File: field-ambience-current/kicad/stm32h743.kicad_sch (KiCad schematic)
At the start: 22 parts, among them J9 JST PH 2.0 2-pin (LiPo Batter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, Q1 DMG2305UX P-MOS SOT-23 (USB-C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, U7 MCP73831T-2ACI/OT (LiPo Charg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, U8 TPS61089RNR (Boost LiPo→5V, 2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

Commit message: pcb(r18.5): Schematic-Migration Phase 3 — STM32H743 + LCD im Generator, Repo-Audit-Fixes
KERN: generate_kicad_project.py erzeugt jetzt die H7-Architektur.

NEU stm32h743.kicad_sch (ersetzt pico.kicad_sch -> kicad/legacy_pico2/):
- 100-Pin-Symbol 1:1 aus offizieller KiCad-Lib (MCU_ST_STM32H7),
  doppelt verifiziert gegen SPEC v0.7 §5 / DS12110 Rev 5 Table 8 —
  alle 52 belegten Zuordnungen identisch (zwei unabhängige Quellen)
- alle SPEC-§5-Netze verdrahtet, 48 Reserve-GPIOs no_connect
- Support: HSE Y1 ABLS-8.000MHZ-B4-T (C596838) + 2x22pF, VCAP 2x2.2uF
  (DS12110 Tab.24), 5x(4.7uF+100nF) VDD-Bank, VDDA-Ferrit C84094 +
  1uF+100nF, BOOT0-PD 10k, NRST-PU 10k+100nF, SWD-J4 (PA13/PA14/GND),
  BAT-Teiler 100k/100k+10nF an PA3, Status-LED PD8, USB-FS PA11/PA12
  (USBLC6-ESD bleibt davor), MIDI_TX-Netz (PD5)

NEU lcd.kicad_sch (ersetzt oled.kicad_sch -> legacy): 8-Pin-ST7789
per SPEC §6 + C6b/C6c + Backlight: PCA9685-Kanal-12 -> LCD_BLK_PWM ->
2N7002 Low-Side + 100k-PD. Netze OLED_* -> LCD_*.

power_tree: U5 AP7361A-33 LDO (+5V->+3V3) + Cin 1uF/Cout 2.2uF +
EN->IN. Pico-SMPS entfällt. PICO_USB_* -> USB_DM/USB_DP.

mcp: GPB5 = VOL_SW (SPEC §5.4 — lag bis r17 entgegen der SPEC am
Pico-GPIO), PCA-Kanal 12 = LCD_BLK_PWM. Root-Brücken umgebaut,
kicad_pro-Sheetliste: Battery ergänzt (fehlte).

AUDIT-FINDINGS (verifiziert, nicht aus dem Alt-Audit übernommen):
- F-6 NEU 🔴: SPEC-§4-U5-LCSC C156144 ist ein 910R-WIDERSTAND
  (LCSC-Web verifiziert) — hätte bei JLC einen R als LDO bestückt.
  SPEC korrigiert (Kandidat C150719), Symbol trägt TBD-VERIFY.
- B-LDO 🔴: AP7361A-SOT-89-5-Pinout-Annahme (1=ADJ/NC,2=OUT,3=IN,
  4=GND,5=EN aus AP7361-DS33626-Lesart; A-Datasheet war HTTP 403) —
  als PIN_VERIFY am Symbol + PCB_LAYOUT_STATUS dokumentiert.
- B-SW12 🔴: SW6-10 (HX 12x12) auf ~6mm-TL3342-Pattern — als
  FP_MISMATCH-Property an allen 5 Symbolen markiert.
- F-2-Teilfix: Encoder-MPN -> EC11J1525402, Bourns-PEC11R-PDF nach
  datasheets/legacy/ (falsches Teil); ALPS-Drawing offen.
- F-1: T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
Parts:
- removed C_BAT_HF: 100nF X7R 0603 (Battery-Input HF), Capacitor_SMD:C_0603_1608Metric, symbol Device:C
- removed C_BAT_IN: 22uF X5R 0805 (Battery-Input Bulk), Capacitor_SMD:C_0805_2012Metric, symbol Device:C
- removed C_BOOST_HF: 100nF X7R 0603 (Boost-Output HF), Capacitor_SMD:C_0603_1608Metric, symbol Device:C
- removed C_BOOST_OUT: 22uF X5R 0805 (Boost-Output Bulk), Capacitor_SMD:C_0805_2012Metric, symbol Device:C
- removed C_BOOT: 100nF X7R 0603 (TPS61089 BOOT-SW cap), Capacitor_SMD:C_0603_1608Metric, symbol Device:C
- removed C_COMP: 1nF X7R 0603 (TPS61089 loop-compensation series), Capacitor_SMD:C_0603_1608Metric, symbol Device:C
- removed C_VCC: 1uF X7R 0603 (TPS61089 internal LDO decoupling, d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, Capacitor_SMD:C_0603_1608Metric, symbol Device:C
- removed D3: SS34 40V 3A Schottky (Boost-Out Reverse-Protect), Diode_SMD:D_SMA, symbol Device:D_Schottky
- removed J9: JST PH 2.0 2-pin (LiPo Battery, r9), Connector_JST:JST_PH_S2B-PH-SM4-TB_1x02-1MP_P2.00mm_Horizontal, symbol Connector:Conn_01x02
- removed L1: 2.2uH 5A Shielded 0630 (TPS61089 Boost Inductor), Inductor_SMD:L_0630_6.0x6.0mm, symbol Device:L
- removed LED_CHRG: 0603 amber (LiPo Charging indicator), LED_SMD:LED_0603_1608Metric, symbol Device:LED
- removed Q1: DMG2305UX P-MOS SOT-23 (USB-C Power-Path-Switch), Package_TO_SOT_SMD:SOT-23, symbol Transistor_FET:DMG2305UX
- removed R21: 2k 0603 (MCP73831 R_PROG → 500mA Icharge), Resistor_SMD:R_0603_1608Metric, symbol Device:R
- removed R22: 10k 0603 (Q1 Gate Pull-Down, Default-OFF), Resistor_SMD:R_0603_1608Metric, symbol Device:R
- removed R23: 200k 0603 (TPS61089 FB-Divider Top, Vout=5V targe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, Resistor_SMD:R_0603_1608Metric, symbol Device:R
- removed R24: 39k 0603 (TPS61089 FB-Divider Bottom), Resistor_SMD:R_0603_1608Metric, symbol Device:R
- removed R_CHRG: 1k 0603 (LED_CHRG series), Resistor_SMD:R_0603_1608Metric, symbol Device:R
- removed R_COMP: 22k 0603 (TPS61089 loop-compensation), Resistor_SMD:R_0603_1608Metric, symbol Device:R
- removed R_FSW: 360k 0603 1% (TPS61089 Fsw-Set ~1.21MHz, r12-B11), Resistor_SMD:R_0603_1608Metric, symbol Device:R
- removed R_ILIM: 20k 0603 1% (TPS61089 current-limit ~4A peak), Resistor_SMD:R_0603_1608Metric, symbol Device:R
- removed U7: MCP73831T-2ACI/OT (LiPo Charger, 500mA via R21=2k), Package_TO_SOT_SMD:SOT-23-5, symbol Battery:MCP73831
- removed U8: TPS61089RNR (Boost LiPo→5V, 2A, programmable Fsw), Package_DFN_QFN:VQFN-11-1EP_2.6x2.6mm_P0.5mm_EP0.85x1.5mm_HotRod, symbol Regulator_Switching:TPS61089
- added C_BAT_FILT: 10nF X7R 0603 (ADC S/H filter), Capacitor_SMD:C_0603_1608Metric, symbol Device:C
- added C_HSE1, C_HSE2: 22pF C0G/NP0 0603 (HSE load, Startwert §5.9), Capacitor_SMD:C_0603_1608Metric, symbol Device:C
- added C_NRST: 100nF X7R 0603 (NRST debounce), Capacitor_SMD:C_0603_1608Metric, symbol Device:C
- added C_VCAP1, C_VCAP2: 2.2uF X5R 0603, ESR<100mOhm (VCAP, DS12110 Tab.24), Capacitor_SMD:C_0603_1608Metric, symbol Device:C
- added C_VDD1A, C_VDD2A, C_VDD3A, C_VDD4A, C_VDD5A: 4.7uF X5R 0805 (VDD bulk), Capacitor_SMD:C_0805_2012Metric, symbol Device:C
- added C_VDD1B, C_VDD2B, C_VDD3B, C_VDD4B, C_VDD5B: 100nF X7R 0603 (VDD HF), Capacitor_SMD:C_0603_1608Metric, symbol Device:C
- added C_VDDA1: 1uF X5R 0603 (VDDA), Capacitor_SMD:C_0603_1608Metric, symbol Device:C
- added C_VDDA2: 100nF X7R 0603 (VDDA), Capacitor_SMD:C_0603_1608Metric, symbol Device:C
- added FB2: BLM18AG601 600R@100MHz (VDDA-Filter), Inductor_SMD:L_0603_1608Metric, symbol Device:Ferrite_Bead
- added J4: SWD 1.27mm (SWCLK/GND/SWDIO), Connector_PinHeader_1.27mm:PinHeader_1x03_P1.27mm_Vertical, symbol Connector:Conn_01x03
- added LED_HB: 0603 warm-white (heartbeat), LED_SMD:LED_0603_1608Metric, symbol Device:LED
- added R_BAT_DIV_BOT: 100k 0603 (BAT divider bottom), Resistor_SMD:R_0603_1608Metric, symbol Device:R
- added R_BAT_DIV_TOP: 100k 0603 (BAT divider top), Resistor_SMD:R_0603_1608Metric, symbol Device:R
- added R_BOOT0: 10k 0603 (BOOT0 pull-down), Resistor_SMD:R_0603_1608Metric, symbol Device:R
- added R_NRST: 10k 0603 (NRST pull-up), Resistor_SMD:R_0603_1608Metric, symbol Device:R
- added R_SLED: 820R 0603 (status LED), Resistor_SMD:R_0603_1608Metric, symbol Device:R
- added U1: STM32H743VIT6 (480MHz M7, LQFP-100), Package_QFP:LQFP-100_14x14mm_P0.5mm, symbol MCU:STM32H743VIT6
- added Y1: 8MHz ABLS-8.000MHZ-B4-T (CL=18pF, ESR<=80R), Crystal:Crystal_SMD_HC49-SD, symbol Device:Crystal
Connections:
- net BAT_PLUS: now also R_BAT_DIV_TOP.1
- net GND: now also C_BAT_FILT.2, C_HSE1.2, C_HSE2.2, C_NRST.2, C_VCAP1.2, C_VCAP2.2, C_VDD1A.2, C_VDD1B.2, C_VDD2A.2, C_VDD2B.2, C_VDD3A.2, C_VDD3B.2, C_VDD4A.2, C_VDD4B.2, C_VDD5A.2, C_VDD5B.2, C_VDDA1.2, C_VDDA2.2, LED_HB.1 (K), R_BAT_DIV_BOT.2, R_BOOT0.2
- new net: LED_HB.2 (A), R_SLED.2
- new net +3V3: C_VDD1A.1, C_VDD1B.1, C_VDD2A.1, C_VDD2B.1, C_VDD3A.1, C_VDD3B.1, C_VDD4A.1, C_VDD4B.1, C_VDD5A.1, C_VDD5B.1, R_NRST.1
- new net BAT_SENSE: C_BAT_FILT.1, R_BAT_DIV_BOT.1, R_BAT_DIV_TOP.2
- new net BOOT0_PIN: R_BOOT0.1
- new net HSE_IN: C_HSE1.1, Y1.1
- new net HSE_OUT: C_HSE2.1, Y1.2
- new net NRST: C_NRST.1, R_NRST.2
- new net STATUS_LED: R_SLED.1
- new net VDDA_3V3: C_VDDA1.1, C_VDDA2.1
- no-connect marks 0 -> 49
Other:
- note added: "MIDI_TX (PD5): Netz vorhanden, TRS-Type-A-Buchse + Serien-R fehlen im Design — SPEC §4 hat keine Buchsen-Zeile. BLOCKER B-MIDI in PCB_TODO.md (MIDI-1.0-3V3-Spec: 10R/33R)."
- note added: "SWO (PB3): optionaler Trace-Pin, bewusst nur Label (ERC-Info erwartet)."
- title: Field Ambience PCB — Sheet 7: Battery & Power-Path (r9 + r12) -> Field Ambience — Sheet 2: STM32H743 (r18 H7-Migration)

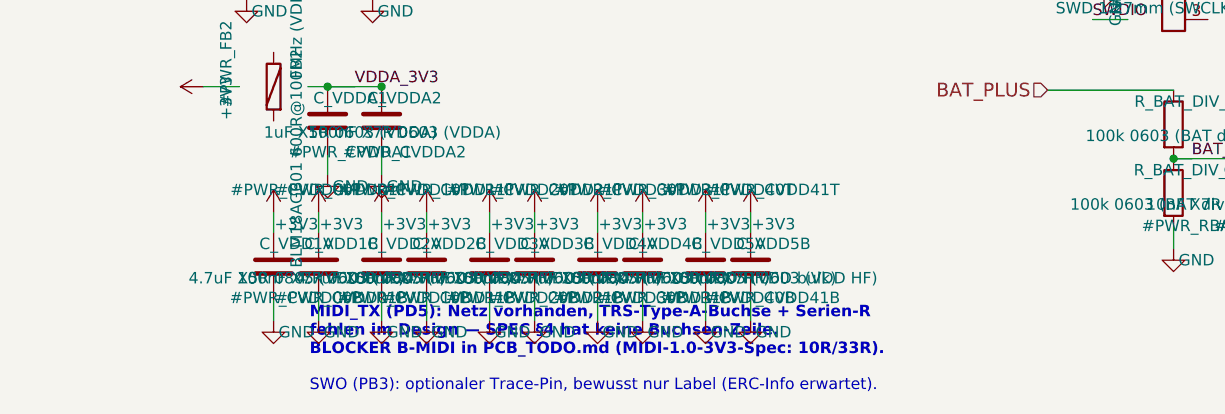
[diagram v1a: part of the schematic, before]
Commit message: pcb(r18.6): Engineering-Verifikation — AP7361C-Pinout-Fix, TPS61089-Quelle, Custom-FP, BOM-LCSC, ADR-MIDI
Reaktion auf User-Korrekturen aus öffentlichen Datasheets. Vier
🔴-Blocker geschlossen, einer auf eine Design-Entscheidung umklassifiziert.

=== AP7361A-Pinout war FALSCH — gefixt + AP7361C ===

r18.5-Annahme: 1=ADJ/NC, 2=OUT, 3=IN, 4=GND, 5=EN.
Korrekt (Diodes-DS via mouser.de/datasheet/3/175/1/AP7361.pdf,
User-verifiziert):
    1=EN, 2=GND, 3=ADJ/NC, 4=IN, 5=OUT

Hätte zu einem totem Board geführt (IN/OUT/EN vertauscht).

Zusätzlich:
- Symbol auf AP7361C umbenannt (Diodes markiert AP7361 als NRND ->
  use AP7361C; gleicher SOT-89-5-Pinout)
- AP7361C-33Y5-13 = LCSC C460397 (SOT-89-5) statt r18.5-Kandidat
  C150719 (= SOT-223, falsches Package; verworfen)
- Cin/Cout 4.7 µF X5R 0603 (DS-Empfehlung, statt 1µF/2.2µF)
- Symbol-Pinmap + power_tree-Verdrahtung umgebaut: EN-Pin liegt
  jetzt links oben (statt links unten), IN links unten, OUT
  rechts oben — neu gerechnete Stub-Wires + Junctions

=== TPS61089-Footprint + Datenblatt-Anchor ===

- Symbol-Pinmap (1=FSW … 11=SW) verifiziert gegen TI Rev C Tabelle 6-1
  (User-Quelle ti.com/lit/gpn/tps61089) — als PIN_SOURCE-Property
- Footprint-Name auf RNR0011A-Konvention 2.0x2.5mm VQFN-HR
- RNSR-PDF → datasheets/legacy/TPS61089RNSR_wrong_variant.pdf

=== Encoder C209762 (NRND, Prototype-OK) ===

- MPN EC11J1525402, LCSC C209762 (JLCPCB-verifiziert)
- Datasheet-Link auf JLCPCB-Detail-Seite (ALPS-Drawing nicht öffentlich)
- Status: NRND als Property — Prototype-OK, Serie braucht Ersatztyp
- FP_VERIFY-Hinweis (EC11J ist SMD, der KiCad-Standard-FP EC11E ist THT)

=== Custom-Footprint für HX 12x12 (SW6-10) ===

- libraries/field_ambience.pretty/SW_HX_12x12x7.3_SMD-4P.kicad_mod
  basierend auf LCSC-Daten von C36498966:
  - SMD-4P, 11.8x11.8mm Body, 7.3mm Höhe
  - 4 Pads je 2.5x1.5mm auf 7mm-Pitch (X+Y)
  - SPST: gegenüberliegende Pads verbunden (1↔1, 2↔2)
  - Silkscreen + Pin-1-Dot + Courtyard +0.25mm IPC-7351B
- fp-lib-table um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
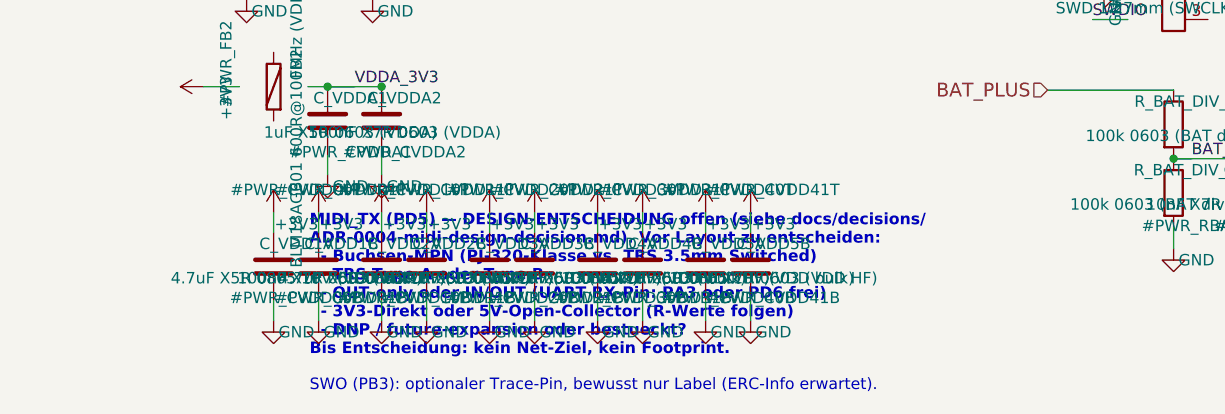
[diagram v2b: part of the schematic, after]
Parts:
- C_HSE1, C_HSE2: LCSC TBD-VERIFY -> C1804; MPN TBD-VERIFY (22pF C0G 50V 0603) -> CC0603JRNPO9BN220; Manufacturer (none) -> Yageo; VERIFY-STOCK (none) -> 22pF +-5% C0G/NP0 50V 0603
- C_VCAP1, C_VCAP2: LCSC TBD-VERIFY -> C24539; MPN TBD-VERIFY (2.2uF/6.3V X5R 0603) -> CL10A225KP8NNNC; Manufacturer (none) -> Samsung; VERIFY-STOCK (none) -> JLC Extended 2.2uF/10V X5R 0603 — falls out-of-stock altern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
- C_VDD1A, C_VDD2A, C_VDD3A, C_VDD4A, C_VDD5A: value 4.7uF X5R 0805 (VDD bulk) -> 4.7uF X5R 0805 10V (VDD bulk); LCSC TBD-VERIFY -> C45783; MPN TBD-VERIFY (4.7uF/10V X5R 0805) -> CL21A475KQFNNNE
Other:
- note added: "MIDI_TX (PD5) — DESIGN-ENTSCHEIDUNG offen (siehe docs/decisions/ ADR-0004-midi-design-decision.md). Vor Layout zu entscheiden: - Buchsen-MPN (PJ-320-Klasse vs. TRS 3.5mm Switched) - TRS Type A oder Type B - OUT-only oder IN/OUT (UART RX-Pin: PA3 oder PD6 frei) - 3V3-Direkt oder 5V-Open-Collector (R-Werte folgen) - DNP / future-expansion oder bestueckt? Bis Entscheidung: kein Net-Ziel, kein Footpr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"
- note removed: "MIDI_TX (PD5): Netz vorhanden, TRS-Type-A-Buchse + Serien-R fehlen im Design — SPEC §4 hat keine Buchsen-Zeile. BLOCKER B-MIDI in PCB_TODO.md (MIDI-1.0-3V3-Spec: 10R/33R)."
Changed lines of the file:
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@@
       (property "Datasheet" "~" (at 112.14 83.01 0)
         (effects (font (size 1.27 1.27)) hide))
-      (property "MPN" "TBD-VERIFY (2.2uF/6.3V X5R 0603)" (at 114.68 86.82000000000001 0)
-        (effects (font (size 1.27 1.27)) hide))
-      (property "LCSC" "TBD-VERIFY" (at 114.68 88.09 0)
+      (property "MPN" "CL10A225KP8NNNC" (at 114.68 86.82000000000001 0)
+        (effects (font (size 1.27 1.27)) hide))
+      (property "Manufacturer" "Samsung" (at 114.68 88.09 0)
+        (effects (font (size 1.27 1.27)) hide))
+      (property "LCSC" "C24539" (at 114.68 89.36 0)
+        (effects (font (size 1.27 1.27)) hide))
+      (property "VERIFY-STOCK" "JLC Extended 2.2uF/10V X5R 0603 — falls out-of-stock alternative LCSC-Nr. waehlen" (at 114.68 90.63000000000001 0)
         (effects (font (size 1.27 1.27)) hide))
     (instances
@@
       (property "Datasheet" "~" (at 112.14 85.55 0)
         (effects (font (size 1.27 1.27)) hide))
-      (property "MPN" "TBD-VERIFY (2.2uF/6.3V X5R 0603)" (at 114.68 89.36 0)
-        (effects (font (size 1.27 1.27)) hide))
-      (property "LCSC" "TBD-VERIFY" (at 114.68 90.63 0)
+      (property "MPN" "CL10A225KP8NNNC" (at 114.68 89.36 0)
+        (effects (font (size 1.27 1.27)) hide))
+      (property "Manufacturer" "Samsung" (at 114.68 90.63 0)
+        (effects (font (size 1.27 1.27)) hide))
+      (property "LCSC" "C24539" (at 114.68 91.89999999999999 0)
+        (effects (font (size 1.27 1.27)) hide))
+      (property "VERIFY-STOCK" "JLC Extended 2.2uF/10V X5R 0603 — falls out-of-stock alternative LCSC-Nr. waehlen" (at 114.68 93.17 0)
         (effects (font (size 1.27 1.27)) hide))
     (instances
@@
       (property "Reference" "C_VDD1A" (at 98.54 235.46 0)
         (effects (font (size 1.27 1.27))))
-      (property "Value" "4.7uF X5R 0805 (VDD bulk)" (at 98.54 239.27 0)
+      (property "Value" "4.7uF X5R 0805 10V (VDD bulk)" (at 98.54 239.27 0)
         (effects (font (size 1.27 1.27))))
       (property "Footprint" "Capacitor_SMD:C_0805_2012Metric" (at 96.0 238.0 0)
@@
       (property "Datasheet" "~" (at 96.0 238.0 0)
         (effects (font (size 1.27 1.27)) hide))
-      (property "MPN" "TBD-VERIFY (4.7uF/10V X5R 0805)" (at 98.54 241.81 0)
-        (effects (font (size 1.27 1.27)) hide))
-      (property "LCSC" "TBD-VERIFY" (at 98.54 243.08 0)
+      (property "MPN" "CL21A475KQFNNNE" (at 98.54 241.81 0)
+        (effects (font (size 1.27 1.27)) hide))
+      (property "LCSC" "C45783" (at 98.54 243.08 0)
         (effects (font (size 1.27 1.27)) hide))
     (instances
@@
       (property "Reference" "C_VDD2A" (at 110.54 235.46 0)
         (effects (font (size 1.27 1.27))))
-      (property "Value" "4.7uF X5R 0805 (VDD bulk)" (at 110.54 239.27 0)
+      (property "Value" "4.7uF X5R 0805 10V (VDD bulk)" (at 110.54 239.27 0)
         (effects (font (size 1.27 1.27))))
       (property "Footprint" "Capacitor_SMD:C_0805_2012Metric" (at 108.0 238.0 0)
@@
       (property "Datasheet" "~" (at 108.0 238.0 0)
         (effects (font (size 1.27 1.27)) hide))
-      (property "MPN" "TBD-VERIFY (4.7uF/10V X5R 0805)" (at 110.54 241.81 0)
-        (effects (font (size 1.27 1.27)) hide))
-      (property "LCSC" "TBD-VERIFY" (at 110.54 243.08 0)
+      (property "MPN" "CL21A475KQFNNNE" (at 110.54 241.81 0)
+        (effects (font (size 1.27 1.27)) hide))
+      (property "LCSC" "C45783" (at 110.54 243.08 0)
         (effects (font (size 1.27 1.27)) hide))
     (instances
@@
       (property "Reference" "C_VDD3A" (at 122.54 235.46 0)
         (effects (font (size 1.27 1.27))))
-      (property "Value" "4.7uF X5R 0805 (VDD bulk)" (at 122.54 239.27 0)
+      (property "Value" "4.7uF X5R 0805 10V (VDD bulk)" (at 122.54 239.27 0)
         (effects (font (size 1.27 1.27))))
       (property "Footprint" "Capacitor_SMD:C_0805_2012Metric" (at 120.0 238.0 0)
@@
       (property "Datasheet" "~" (at 120.0 238.0 0)
         (effects (font (size 1.27 1.27)) hide))
-      (property "MPN" "TBD-VERIFY (4.7uF/10V X5R 0805)" (at 122.54 241.81 0)
-        (effects (font (size 1.27 1.27)) hide))
-      (property "LCSC" "TBD-VERIFY" (at 122.54 243.08 0)
+      (property "MPN" "CL21A475KQFNNNE" (at 122.54 241.81 0)
+        (effects (font (size 1.27 1.27)) hide))
+      (property "LCSC" "C45783" (at 122.54 243.08 0)
         (effects (font (size 1.27 1.27)) hide))
     (instances
@@
       (property "Reference" "C_VDD4A" (at 134.54 235.46 0)
         (effects (font (size 1.27 1.27))))
-      (property "Value" "4.7uF X5R 0805 (VDD bulk)" (at 134.54 239.27 0)
+      (property "Value" "4.7uF X5R 0805 10V (VDD bulk)" (at 134.54 239.27 0)
         (effects (font (size 1.27 1.27))))
       (property "Footprint" "Capacitor_SMD:C_0805_2012Metric" (at 132.0 238.0 0)
@@
       (property "Datasheet" "~" (at 132.0 238.0 0)
         (effects (font (size 1.27 1.27)) hide))
-      (property "MPN" "TBD-VERIFY (4.7uF/10V X5R 0805)" (at 134.54 241.81 0)
-        (effects (font (size 1.27 1.27)) hide))
-      (property "LCSC" "TBD-VERIFY" (at 134.54 243.08 0)
+      (property "MPN" "CL21A475KQFNNNE" (at 134.54 241.81 0)
+        (effects (font (size 1.27 1.27)) hide))
+      (property "LCSC" "C45783" (at 134.54 243.08 0)
         (effects (font (size 1.27 1.27)) hide))
     (instances
@@
       (property "Reference" "C_VDD5A" (at 146.54 235.46 0)
         (effects (font (size 1.27 1.27))))
-      (property "Value" "4.7uF X5R 0805 (VDD bulk)" (at 146.54 239.27 0)
+      (property "Value" "4.7uF X5R 0805 10V (VDD bulk)" (at 146.54 239.27 0)
         (effects (font (size 1.27 1.27))))
       (property "Footprint" "Capacitor_SMD:C_0805_2012Metric" (at 144.0 238.0 0)
@@
       (property "Datasheet" "~" (at 144.0 238.0 0)
         (effects (font (size 1.27 1.27)) hide))
-      (property "MPN" "TBD-VERIFY (4.7uF/10V X5R 0805)" (at 146.54 241.81 0)
-        (effects (font (size 1.27 1.27)) hide))
-      (property "LCSC" "TBD-VERIFY" (at 146.54 243.08 0)
+      (property "MPN" "CL21A475KQFNNNE" (at 146.54 241.81 0)
+        (effects (font (size 1.27 1.27)) hide))
+      (property "LCSC" "C45783" (at 146.54 243.08 0)
         (effects (font (size 1.27 1.27)) hide))
     (instances
@@
       (property "Datasheet" "~" (at 93.0 202.35 0)
         (effects (font (size 1.27 1.27)) hide))
-      (property "MPN" "TBD-VERIFY (22pF C0G 50V 0603)" (at 95.54 206.16 0)
-        (effects (font (size 1.27 1.27)) hide))
-      (property "LCSC" "TBD-VERIFY" (at 95.54 207.43 0)
+      (property "MPN" "CC0603JRNPO9BN220" (at 95.54 206.16 0)
+        (effects (font (size 1.27 1.27)) hide))
+      (property "Manufacturer" "Yageo" (at 95.54 207.43 0)
+        (effects (font (size 1.27 1.27)) hide))
+      (property "LCSC" "C1804" (at 95.54 208.7 0)
+        (effects (font (size 1.27 1.27)) hide))
+      (property "VERIFY-STOCK" "22pF +-5% C0G/NP0 50V 0603" (at 95.54 209.97 0)
         (effects (font (size 1.27 1.27)) hide))
     (instances
@@
       (property "Datasheet" "~" (at 107.0 202.35 0)
         (effects (font (size 1.27 1.27)) hide))
-      (property "MPN" "TBD-VERIFY (22pF C0G 50V 0603)" (at 109.54 206.16 0)
-        (effects (font (size 1.27 1.27)) hide))
-      (property "LCSC" "TBD-VERIFY" (at 109.54 207.43 0)
+      (property "MPN" "CC0603JRNPO9BN220" (at 109.54 206.16 0)
+        (effects (font (size 1.27 1.27)) hide))
+      (property "Manufacturer" "Yageo" (at 109.54 207.43 0)
+        (effects (font (size 1.27 1.27)) hide))
+      (property "LCSC" "C1804" (at 109.54 208.7 0)
+        (effects (font (size 1.27 1.27)) hide))
+      (property "VERIFY-STOCK" "22pF +-5% C0G/NP0 50V 0603" (at 109.54 209.97 0)
         (effects (font (size 1.27 1.27)) hide))
     (instances
@@
   (no_connect (at 142.54 201.12)
 )
-  (text "MIDI_TX (PD5): Netz vorhanden, TRS-Type-A-Buchse + Serien-R\nfehlen im Design — SPEC §4 hat keine Buchsen-Zeile.\nBLOCKER B-MIDI in PCB_TODO.md (MIDI-1.0-3V3-Spec: 10R/33R)." (at 100 248 0)
+  (text "MIDI_TX (PD5) — DESIGN-ENTSCHEIDUNG offen (siehe docs/decisions/\nADR-0004-midi-design-decision.md). Vor Layout zu entscheiden:\n  - Buchsen-MPN (PJ-320-Klasse vs. TRS 3.5mm Switched)\n  - TRS Type A oder Type B\n  - OUT-only oder IN/OUT (UART RX-Pin: PA3 oder PD6 frei)\n  - 3V3-Direkt oder 5V-Open-Collector (R-Werte folgen)\n  - DNP / future-expansion oder bestueckt?\nBis Entscheidung: kein Net-Ziel, kein Footprint." (at 100 248 0)
     (effects (font (size 1.27 1.27) bold) (justify left bottom))
 )
